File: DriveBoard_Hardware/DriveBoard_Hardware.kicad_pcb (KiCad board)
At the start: 2 copper layers, 61 x 91.2 mm, 12 parts, among them U1 TM4C129E_Launchpad, U2 MAX_3232, U3 OKI

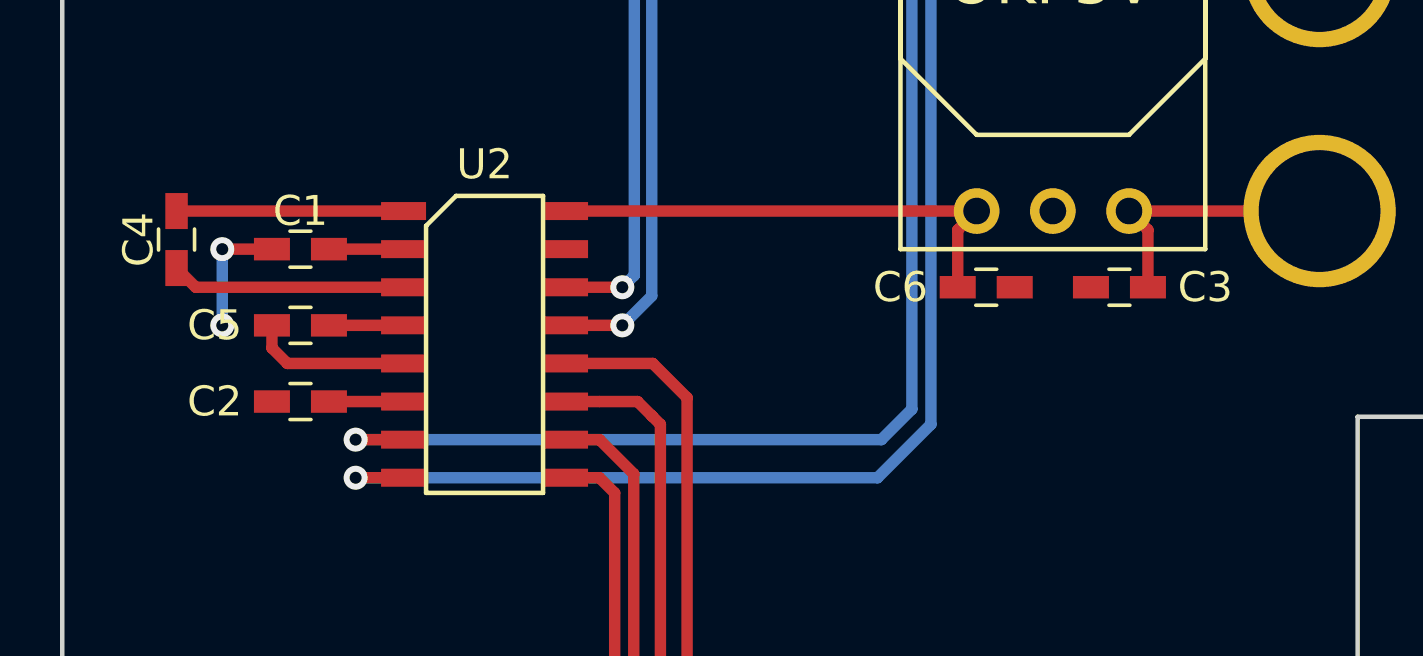
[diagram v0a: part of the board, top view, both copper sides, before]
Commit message: Changed Footprint Mapping to KiCAD 5.0
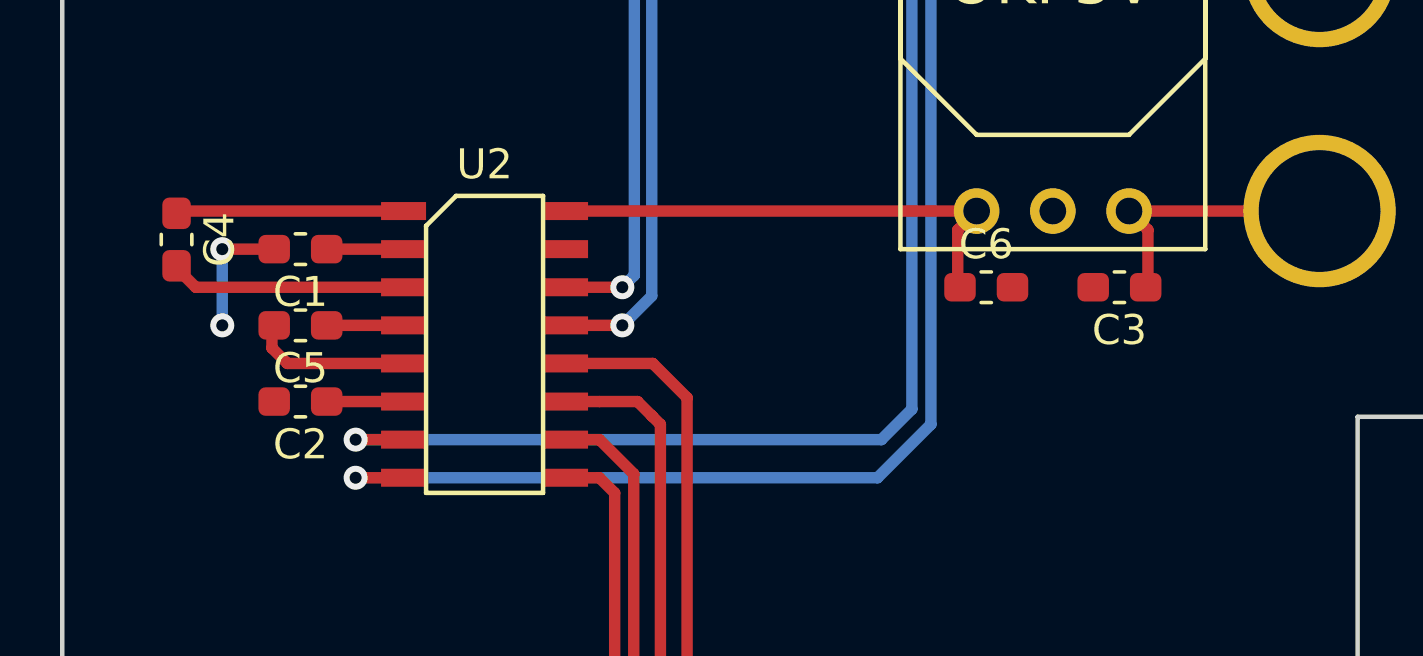
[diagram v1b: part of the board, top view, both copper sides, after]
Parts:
- C1, C2, C3, C4, C5, C6: footprint Capacitors_SMD:C_0603_HandSoldering -> Capacitor_SMD:C_0603_1608Metric_Pad1.05x0.95mm_HandSolder

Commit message: Generated Gerbs and BOM
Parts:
- moved C2 80.1 mm to (95.6, 106.7)
- moved Conn1 80.1 mm to (133.1, 88.3)
- moved Conn3 80.1 mm to (115.6, 74.9)
- moved C1 80.1 mm to (95.6, 101.6)
- moved C3 80.1 mm to (122.9, 102.9)
- moved C4 80.1 mm to (91.4, 101.3)
- moved C5 80.1 mm to (95.6, 104.1)
- moved C6 80.1 mm to (118.4, 102.9)
- moved Conn2 80.1 mm to (96.5, 74.9)
- moved U1 80.1 mm to (87.6, 127.5)
- moved U2 80.1 mm to (101.7, 104.8)
- moved U3 80.1 mm to (125.7, 101.6)

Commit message: Board Layout Completed
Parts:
- removed C6: 10uF, Capacitor_SMD:C_0603_1608Metric_Pad1.05x0.95mm_HandSolder
- added G***: LOGO, MRDT_Silkscreens:MRDT_Logo_20mm, F.Cu at (222.5, 156.0)
- moved Conn2 105.2 mm to (200.7, 90.2)
- moved U3 91.9 mm to (215.9, 119.4), turned to 90 degrees
- moved C3 91.3 mm to (213.2, 116.0), turned to 270 degrees
- moved C4 89.8 mm to (178.6, 123.1)
- moved C1 88.2 mm to (181.9, 119.6)
- moved U1 88.1 mm to (174.3, 143.3)
- moved C2 88.0 mm to (178.8, 135.3), turned to 270 degrees
- moved C5 86.2 mm to (178.6, 127.3), turned to 270 degrees
- moved U2 84.9 mm to (183.6, 126.9)
- moved Conn1 83.1 mm to (215.9, 95.2), turned to 270 degrees
- moved Conn3 69.0 mm to (182.9, 90.2)
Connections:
- Conn2 pad 1: (no net) -> Net-(Conn2-Pad1)
- Conn2 pad 2: (no net) -> Net-(Conn2-Pad2)
- Conn3 pad 1: (no net) -> Net-(Conn3-Pad1)
- Conn3 pad 2: (no net) -> Net-(Conn3-Pad2)
- U1 pad +3V3: (no net) -> Net-(U1-Pad+3V3)
- U1 pad PA4: (no net) -> Net-(U1-PadPA4)
- U1 pad PA5: (no net) -> Net-(U1-PadPA5)
- U1 pad PA7: (no net) -> Net-(U1-PadPA7)
- U1 pad PB4: (no net) -> Net-(U1-PadPB4)
- U1 pad PB5: (no net) -> Net-(U1-PadPB5)
- U1 pad PD2: (no net) -> Net-(U1-PadPD2)
- U1 pad PD4: (no net) -> Net-(U1-PadPD4)
- U1 pad PD5: (no net) -> Net-(U1-PadPD5)
- U1 pad PG1: (no net) -> Net-(U1-PadPG1)
- U1 pad PH0: (no net) -> Net-(U1-PadPH0)
- U1 pad PH1: (no net) -> Net-(U1-PadPH1)
- U1 pad PK2: (no net) -> Net-(U1-PadPK2)
- U1 pad PK3: (no net) -> Net-(U1-PadPK3)
- U1 pad PK4: (no net) -> Net-(U1-PadPK4)
- U1 pad PK5: (no net) -> Net-(U1-PadPK5)
- U1 pad PK6: (no net) -> Net-(U1-PadPK6)
- U1 pad PK7: (no net) -> Net-(U1-PadPK7)
- U1 pad PM0: (no net) -> Net-(U1-PadPM0)
- U1 pad PM1: (no net) -> Net-(U1-PadPM1)
- U1 pad PM2: (no net) -> Net-(U1-PadPM2)
- U1 pad PM6: (no net) -> Net-(U1-PadPM6)
- U1 pad PM7: (no net) -> Net-(U1-PadPM7)
- U1 pad PN4: (no net) -> Net-(U1-PadPN4)
- U1 pad PN5: (no net) -> Net-(U1-PadPN5)
- U1 pad PP3: (no net) -> Net-(U1-PadPP3)
- U1 pad PP4: (no net) -> Net-(U1-PadPP4)
- U1 pad PP5: (no net) -> Net-(U1-PadPP5)
- U1 pad PQ0: (no net) -> Net-(U1-PadPQ0)
- U1 pad PQ1: (no net) -> Net-(U1-PadPQ1)
- U1 pad PQ2: (no net) -> Net-(U1-PadPQ2)
- U1 pad PQ3: (no net) -> Net-(U1-PadPQ3)
- U1 pad Rese: (no net) -> Net-(U1-PadRese)
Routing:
- net RX_1_SL: track 35.8 -> 55.9 mm
- net /+12V: track 9.15 -> 27.1 mm
- net RX_1_IC: track 36.4 -> 18.7 mm
- net TX_1_IC: track 31.8 -> 15.5 mm
- net TX_1_SL: track 36.5 -> 52.5 mm
- net RX_2_IC: track 22.2 -> 8.86 mm, vias 0 -> 1
- net +5V: track 16.5 -> 5.36 mm, vias 0 -> 1
- net TX_2_IC: track 21.8 -> 11.4 mm, vias 0 -> 1
- net RX_2_SL: track 57.1 -> 50.0 mm, vias 1 -> 0
- net Net-(C2-Pad1): track 2.49 -> 9.52 mm
- net TX_2_SL: track 53.5 -> 47.2 mm
- net Net-(C4-Pad1): track 7.57 -> 2.48 mm
- net Net-(C4-Pad2): track 7.83 -> 2.81 mm
- net GND: track 4.20 -> 0.41 mm, vias 2 -> 0
- net Net-(C1-Pad1): track 2.49 -> 5.47 mm
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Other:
- board size 61 x 91.2 mm -> 61 x 91.9 mm
- board text added: "12 V"
- board text added: "Drive Board Rev1 Mars Rover Design Team Missouri S&T Brian Kaufman"
- board text added: "GND"
- board text removed: "OKI 5V"
- board text removed: "Training Board, Rev 1 Mars Rover 2018 Missouri S&T Andrew Van Horn"
